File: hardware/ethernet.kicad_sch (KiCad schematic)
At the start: 3 parts, among them J1 Conn_02x03_Odd_Even, J2 Conn_01x16, J3 Conn_01x12

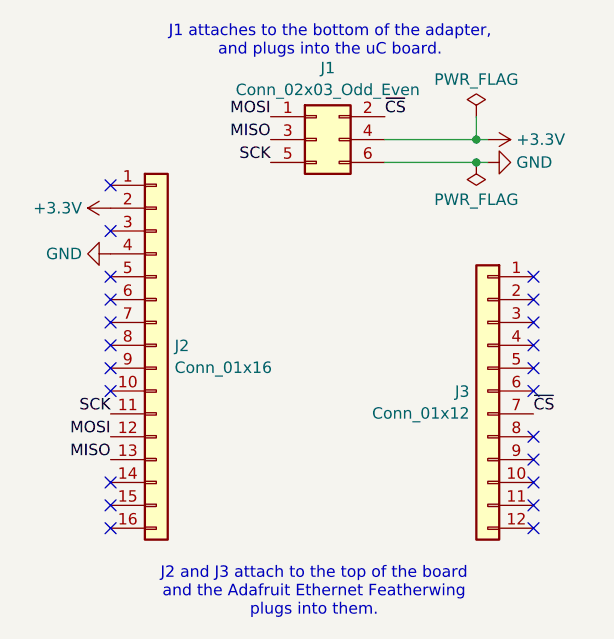
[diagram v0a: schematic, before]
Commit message: Correct placement of bottom-facing header on Ethernet adapter board
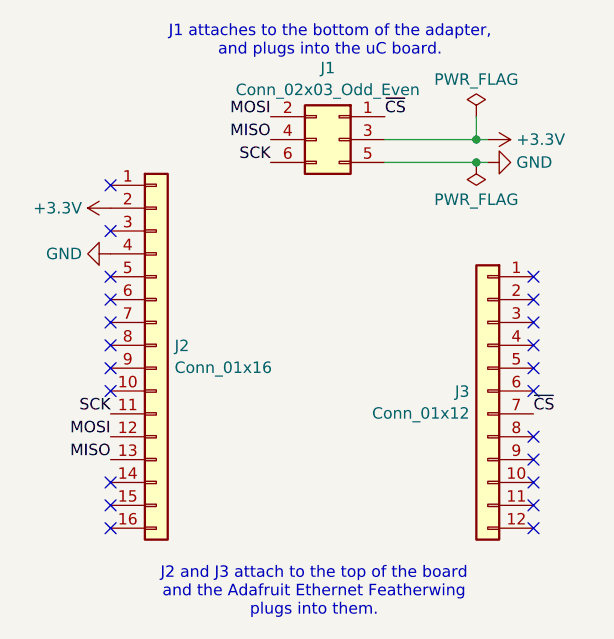
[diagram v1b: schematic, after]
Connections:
- net +3.3V: now also J1.3 (Pin_3); no longer J1.4 (Pin_4)
- net GND: now also J1.5 (Pin_5); no longer J1.6 (Pin_6)
- net MISO: now also J1.4 (Pin_4); no longer J1.3 (Pin_3)
- net MOSI: now also J1.2 (Pin_2); no longer J1.1 (Pin_1)
- net SCK: now also J1.6 (Pin_6); no longer J1.5 (Pin_5)
- net ~{CS}: now also J1.1 (Pin_1); no longer J1.2 (Pin_2)
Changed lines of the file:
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@@
+	)
+	(symbol
+		(lib_id "Connector_Generic:Conn_02x03_Odd_Even")
+		(at 53.34 38.1 0)
+		(mirror y)
+		(unit 1)
+		(exclude_from_sim no)
+		(in_bom yes)
+		(on_board yes)
+		(dnp no)
+		(property "Reference" "J1"
+			(at 52.07 30.1455 0)
+			(effects
+				(font
+					(size 1.27 1.27)
+				)
+			)
+		)
+		(property "Value" "Conn_02x03_Odd_Even"
+			(at 52.07 32.5698 0)
+			(effects
+				(font
+					(size 1.27 1.27)
+				)
+			)
+		)
+		(property "Footprint" "Connector_PinHeader_2.54mm:PinHeader_2x03_P2.54mm_Vertical"
+			(at 53.34 38.1 0)
+			(effects
+				(font
+					(size 1.27 1.27)
+				)
+				(hide yes)
+			)
+		)
+		(property "Datasheet" "~"
+			(at 53.34 38.1 0)
+			(effects
+				(font
+					(size 1.27 1.27)
+				)
+				(hide yes)
+			)
+		)
+		(property "Description" "Generic connector, double row, 02x03, odd/even pin numbering scheme (row 1 odd numbers, row 2 even numbers), script generated (kicad-library-utils/schlib/autogen/connector/)"
+			(at 53.34 38.1 0)
+			(effects
+				(font
+					(size 1.27 1.27)
+				)
+				(hide yes)
+			)
+		)
+		(property "JLCPCB Part Number" "C7501594"
+			(at 53.34 38.1 0)
+			(effects
+				(font
+					(size 1.27 1.27)
+				)
+				(hide yes)
+			)
+		)
+		(property "Mouser Part Number" "737-PH2-06-UA"
+			(at 53.34 38.1 0)
+			(effects
+				(font
+					(size 1.27 1.27)
+				)
+				(hide yes)
+			)
+		)
+		(property "Part Number" "PH2-06-UA"
+			(at 53.34 38.1 0)
+			(effects
+				(font
+					(size 1.27 1.27)
+				)
+				(hide yes)
+			)
+		)
+		(pin "1"
+		)
+		(pin "6"
+		)
+		(pin "5"
+		)
+		(pin "4"
+		)
+		(pin "3"
+		)
+		(pin "2"
+		)
+		(instances
+			(project "ethernet"
+				(path "/b1dc5e42-aa91-4854-9ce2-fed45471f957"
+					(reference "J1")
+					(unit 1)
+				)
+			)
+		)
 	)
 	(symbol
@@
 					(unit 1)
 				)
-			)
-		)
-	)
-	(symbol
-		(lib_id "Connector_Generic:Conn_02x03_Odd_Even")
-		(at 50.8 38.1 0)
-		(unit 1)
-		(exclude_from_sim no)
-		(in_bom yes)
-		(on_board yes)
-		(dnp no)
-		(fields_autoplaced yes)
-		(property "Reference" "J1"
-			(at 52.07 30.1455 0)
-			(effects
-				(font
-					(size 1.27 1.27)
-				)
-			)
-		)
-		(property "Value" "Conn_02x03_Odd_Even"
-			(at 52.07 32.5698 0)
-			(effects
-				(font
-					(size 1.27 1.27)
-				)
-			)
-		)
-		(property "Footprint" "Connector_PinHeader_2.54mm:PinHeader_2x03_P2.54mm_Vertical"
-			(at 50.8 38.1 0)
-			(effects
-				(font
-					(size 1.27 1.27)
-				)
-				(hide yes)
-			)
-		)
-		(property "Datasheet" "~"
-			(at 50.8 38.1 0)
-			(effects
-				(font
-					(size 1.27 1.27)
-				)
-				(hide yes)
-			)
-		)
-		(property "Description" "Generic connector, double row, 02x03, odd/even pin numbering scheme (row 1 odd numbers, row 2 even numbers), script generated (kicad-library-utils/schlib/autogen/connector/)"
-			(at 50.8 38.1 0)
-			(effects
-				(font
-					(size 1.27 1.27)
-				)
-				(hide yes)
-			)
-		)
-		(property "JLCPCB Part Number" "C7501594"
-			(at 50.8 38.1 0)
-			(effects
-				(font
-					(size 1.27 1.27)
-				)
-				(hide yes)
-			)
-		)
-		(property "Mouser Part Number" "737-PH2-06-UA"
-			(at 50.8 38.1 0)
-			(effects
-				(font
-					(size 1.27 1.27)
-				)
-				(hide yes)
-			)
-		)
-		(property "Part Number" "PH2-06-UA"
-			(at 50.8 38.1 0)
-			(effects
-				(font
-					(size 1.27 1.27)
-				)
-				(hide yes)
-			)
-		)
-		(pin "1"
-		)
-		(pin "6"
-		)
-		(pin "5"
-		)
-		(pin "4"
-		)
-		(pin "3"
-		)
-		(pin "2"
-		)
-		(instances
-			(project ""
-				(path "/b1dc5e42-aa91-4854-9ce2-fed45471f957"
-					(reference "J1")
-					(unit 1)
-				)
